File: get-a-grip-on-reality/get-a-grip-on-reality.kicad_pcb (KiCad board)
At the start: 2 copper layers, 100 x 100 mm, 87 parts, among them J1 Conn_01x04_Pin, J10 MOTOR4, J11 MOTOR5, J12 Battery Connector MCU, J13 Conn_01x05_Pin, J14 Conn_01x05_Pin, J15 Battery Connector Bat, J2 HALL1, J3 HALL2, J4 HALL3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

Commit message: fixes to pcb
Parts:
- added  : LOGO, Symbol:logo_shark, F.Cu at (108.3, 89.5)
- added P2: USB_C_Plug_USB2.0, Connector_USB:USB_C_Receptacle_GCT_USB4110, F.Cu at (123.3, 34.9)
- D8: moved to B.Cu
- moved D8 56.3 mm to (126.2, 42.3)
- moved R8 2.77 mm to (129.5, 53.7)
- moved D7 1.84 mm to (127.5, 54.6), turned to -90 degrees
- moved R12 0.46 mm to (121.3, 68.3)
- moved C24 0.45 mm to (121.3, 64.9)
- moved C21 0.11 mm to (122.2, 55.2)
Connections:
- C14 pad 1: +5V -> +5VUSB
- C28 pad 1: +5V -> +5VBuck
- C29 pad 1: +5V -> +5VBuck
- C30 pad 1: +5V -> +5VBuck
- D7 pad 2: GND -> +5VUSB
- D8 pad 2: +5V -> +5VUSB
- J15 pad 2: +5V -> +5VBuck
- L2 pad 2: +5V -> +5VBuck
- P1 pad A4: +5V -> +5V_USB_ESP
- P1 pad A9: +5V -> +5V_USB_ESP
- P1 pad B4: +5V -> +5V_USB_ESP
- P1 pad B9: +5V -> +5V_USB_ESP
- P1 pad S1: unconnected-(P1-SHIELD-PadS1) -> GND
- R19 pad 1: +5V -> +5VBuck
- U3 pad 4: +5V -> +5V_USB_ESP
- U3 pad 7: +5V -> +5V_USB_ESP
- U6 pad 23: +5V -> +5VUSB
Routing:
- net +5V: track 78.6 -> 0.00 mm, vias 5 -> 3
- net +5VUSB: track 0.00 -> 33.0 mm, vias 0 -> 1
- net +5VBuck: track 0.00 -> 15.9 mm, vias 0 -> 2
- net GND: track 36.3 -> 50.0 mm, vias 226 -> 221
- net +5V_USB_ESP: track 0.00 -> 10.2 mm
- net Net-(U6-STAT): track 3.69 -> 6.96 mm
- net Net-(D7-K): track 1.84 -> 2.77 mm
- net Net-(U6-BTST): track 13.8 -> 13.1 mm
- net Net-(U7-VCC): track 13.0 -> 12.4 mm
- net Net-(P2-D+): track 0.00 -> 0.50 mm
- net +BATT: vias 51 -> 50
- added copper zone on B.Cu, net +5VBuck

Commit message: add more shorks
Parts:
- added  : LOGO, Symbol:logo_shark, B.Cu at (54.3, 70.4)
- added  : LOGO, Symbol:logo_shark, B.Cu at (55.9, 47.5)
- added  : LOGO, Symbol:logo_shark, B.Cu at (68.8, 58.1)
- added  : LOGO, Symbol:logo_shark, B.Cu at (76.8, 39.5)
-  : moved to B.Cu
- turned   to 180 degrees
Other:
- board text added: "Get a Grip on Reality Sherwin Chiu Winston Lu Paul Kokhanov Chris Risebrough Andrew Droujinine"

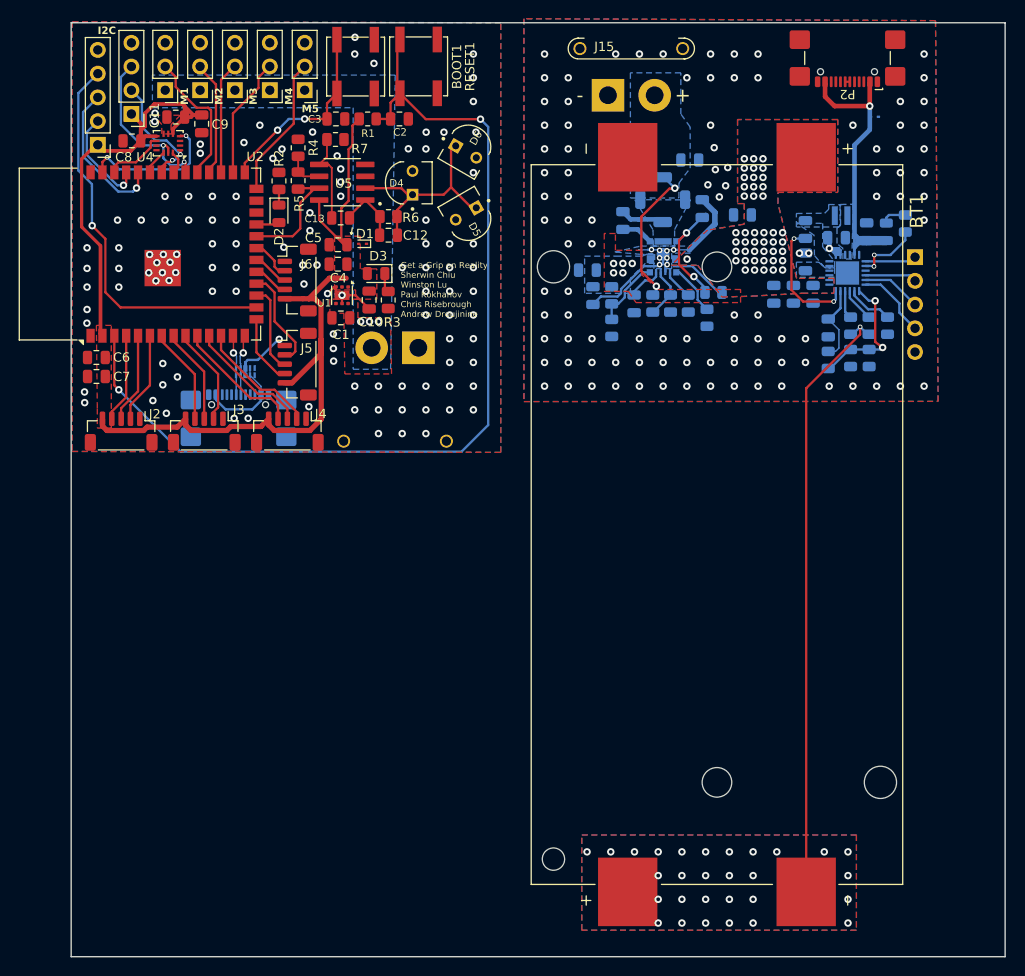
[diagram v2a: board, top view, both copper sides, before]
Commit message: add edge marks separately for pcbs
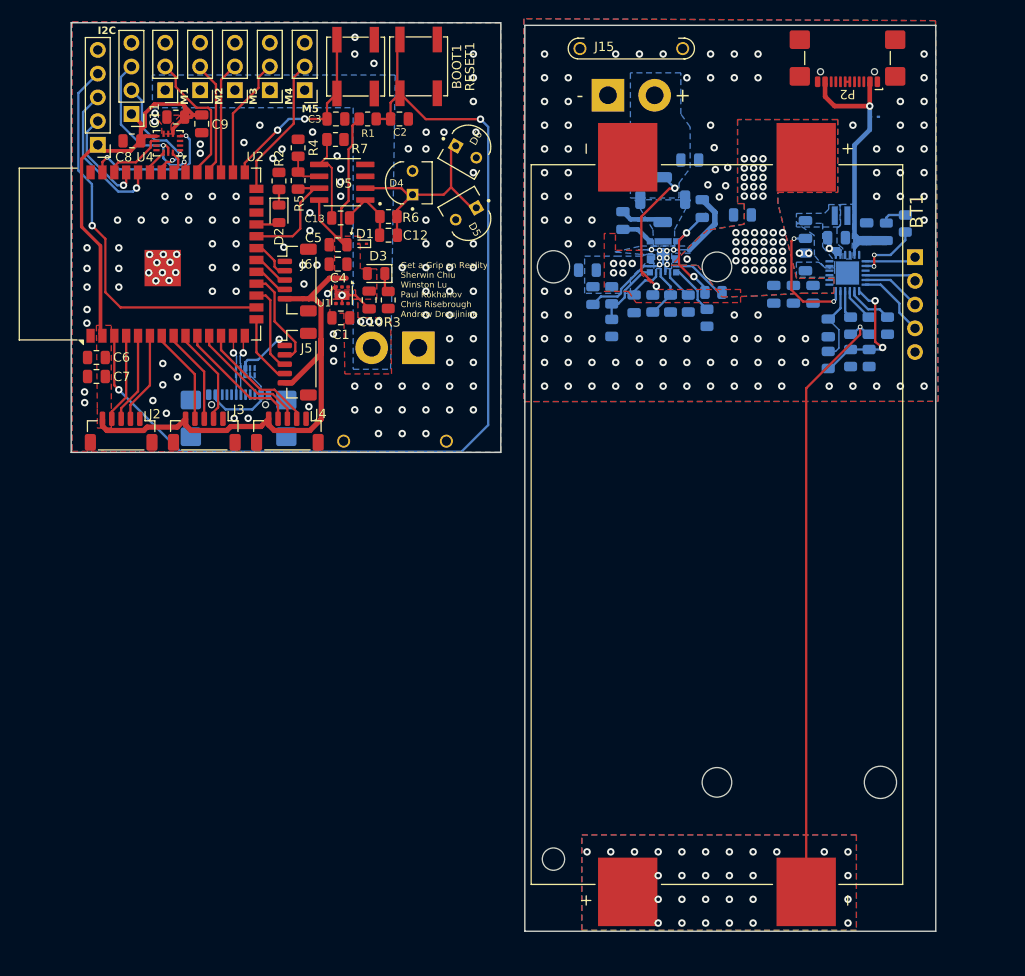
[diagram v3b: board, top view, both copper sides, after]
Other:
- board size 100 x 100 mm -> 92.6 x 97.3 mm
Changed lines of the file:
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@@
 	(gr_rect
 		(start 40.225 32.225)
-		(end 140.225 132.225)
+		(end 86.225 78.225)
 		(stroke
 			(width 0.15)
+			(type default)
+		)
+		(fill none)
+		(layer "Edge.Cuts")
+	)
+	(gr_rect
+		(start 88.8 32.5)
+		(end 132.8 129.5)
+		(stroke
+			(width 0.15)

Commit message: final version
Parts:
- removed the   at (108.3, 89.5)
- removed BT1: 1048P, fydp library:BAT_1048P
- removed C14, C16, C19: 1u, Capacitor_SMD:C_0805_2012Metric
- removed C15, C18, C24: 4.7u, Capacitor_SMD:C_0805_2012Metric
- removed C17, C20, C27: 100n, Capacitor_SMD:C_0805_2012Metric
- removed C21: 10u, Capacitor_SMD:C_0805_2012Metric
- removed C22: 2.2u, Capacitor_SMD:C_0805_2012Metric
- removed C23: 39n, Capacitor_SMD:C_0805_2012Metric
- removed C25: 47n, Capacitor_SMD:C_0805_2012Metric
- removed C26: 44u, Capacitor_SMD:C_0805_2012Metric
- removed C28, C29, C30: 47u, Capacitor_SMD:C_0805_2012Metric
- removed D7: LED, LED_SMD:LED_0805_2012Metric
- removed D8: ESD9B5.0ST5G, Diode_SMD:D_SOD-923
- removed J14: Conn_01x05_Pin, Connector_PinHeader_2.54mm:PinHeader_1x05_P2.54mm_Vertical
- removed J15: Battery Connector Bat, Connector_AMASS:AMASS_XT30PW-F_1x02_P2.50mm_Horizontal
- removed L1: 1u, Inductor_SMD:L_Taiyo-Yuden_MD-2020
- removed L2: 220u, Inductor_SMD:L_Bourns_SRU5016_5.2x5.2mm
- removed P2: USB_C_Plug_USB2.0, Connector_USB:USB_C_Receptacle_GCT_USB4110
- removed R10: 422k, Resistor_SMD:R_0805_2012Metric
- removed R11: 100k, Resistor_SMD:R_0805_2012Metric
- removed R12: 5.23k, Resistor_SMD:R_0805_2012Metric
- removed R13: 30.1k, Resistor_SMD:R_0805_2012Metric
- removed R14, R20, TH1: 10k, Resistor_SMD:R_0805_2012Metric
- removed R15: 11k, Resistor_SMD:R_0805_2012Metric
- removed R16: 5k, Resistor_SMD:R_0805_2012Metric
- removed R17: 300, Resistor_SMD:R_0805_2012Metric
- removed R18: 9.5, Resistor_SMD:R_0805_2012Metric
- removed R19: 45.3k, Resistor_SMD:R_0805_2012Metric
- removed R8: 2.2k, Resistor_SMD:R_0805_2012Metric
- removed R9: 383, Resistor_SMD:R_0805_2012Metric
- removed U6: BQ25887, Package_DFN_QFN:VQFN-24-1EP_4x4mm_P0.5mm_EP2.5x2.5mm
- removed U7: TPS54KB20RZRR, fydp:RZR0016A-MFG
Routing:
- net /Power/CELL_1: track 65.5 -> 0.00 mm, vias 30 -> 0
- net GND: track 50.0 -> 12.9 mm, vias 221 -> 120
- net +5VUSB: track 33.0 -> 0.00 mm, vias 1 -> 0
- net +5VBuck: track 15.9 -> 0.00 mm, vias 2 -> 0
- net Net-(U6-TS): track 14.0 -> 0.00 mm, vias 2 -> 0
- net Net-(U6-BTST): track 13.1 -> 0.00 mm, vias 2 -> 0
- net Net-(U7-VCC): track 12.4 -> 0.00 mm, vias 2 -> 0
- net Net-(U6-REGN): track 8.03 -> 0.00 mm
- net Net-(J14-Pin_4): track 7.81 -> 0.00 mm
- net Net-(U7-EN): track 7.60 -> 0.00 mm
- net Net-(U6-STAT): track 6.96 -> 0.00 mm, vias 2 -> 0
- net Net-(J14-Pin_3): track 6.39 -> 0.00 mm
- net Net-(U7-PG): track 6.10 -> 0.00 mm
- net Net-(J14-Pin_2): track 5.54 -> 0.00 mm
- net Net-(U7-MSEL): track 5.50 -> 0.00 mm
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- removed copper zone on B.Cu, net +5VBuck
- removed copper zone on B.Cu, net +BATT
- removed copper zone on F.Cu, net +BATT
- removed copper zone on B.Cu, net /Power/CELL_1
- removed copper zone on F.Cu, net /Power/CELL_1
- removed copper zone on B.Cu, net /Power/PMID
- removed copper zone on B.Cu, net /Power/SNS
- removed copper zone on B.Cu, net /Power/SW_5
- removed copper zone on B.Cu, net /Power/SW_BAT
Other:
- board size 92.6 x 97.3 mm -> 46 x 46 mm

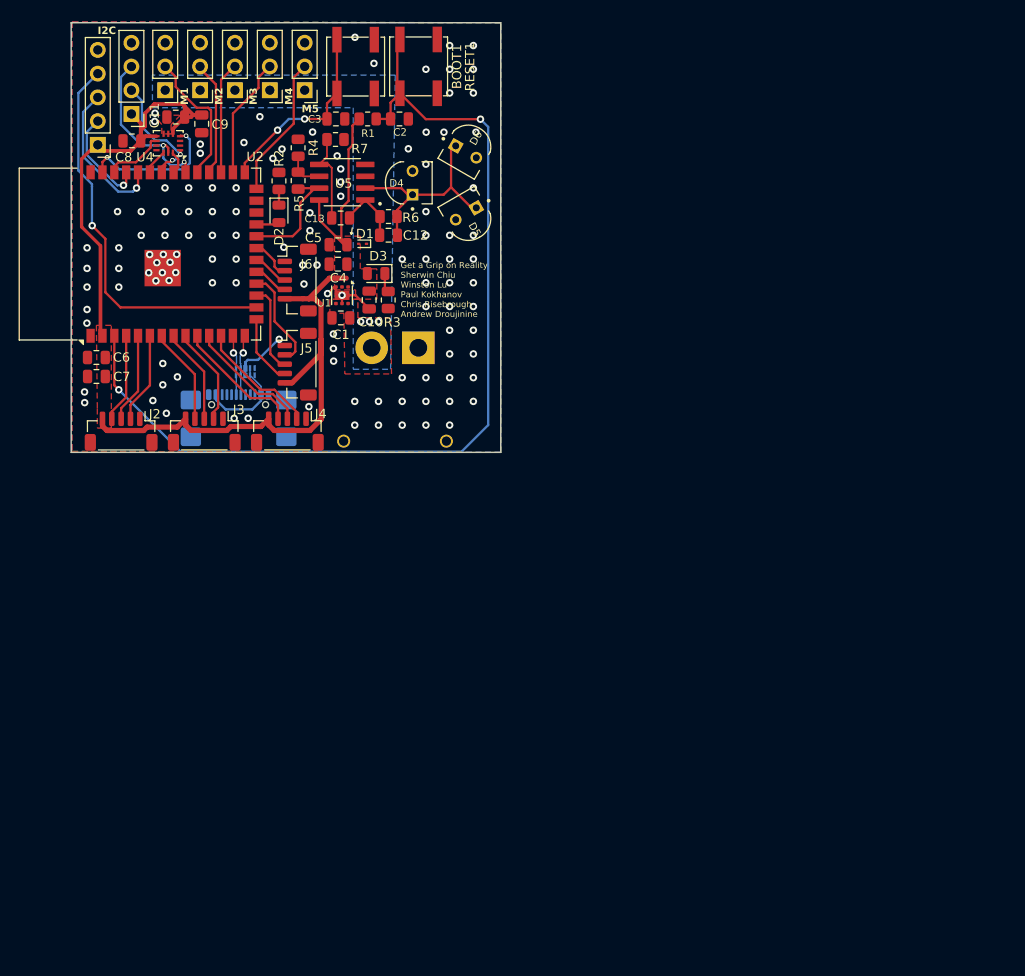
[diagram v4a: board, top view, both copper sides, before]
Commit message: add test.ino for ble and imu test
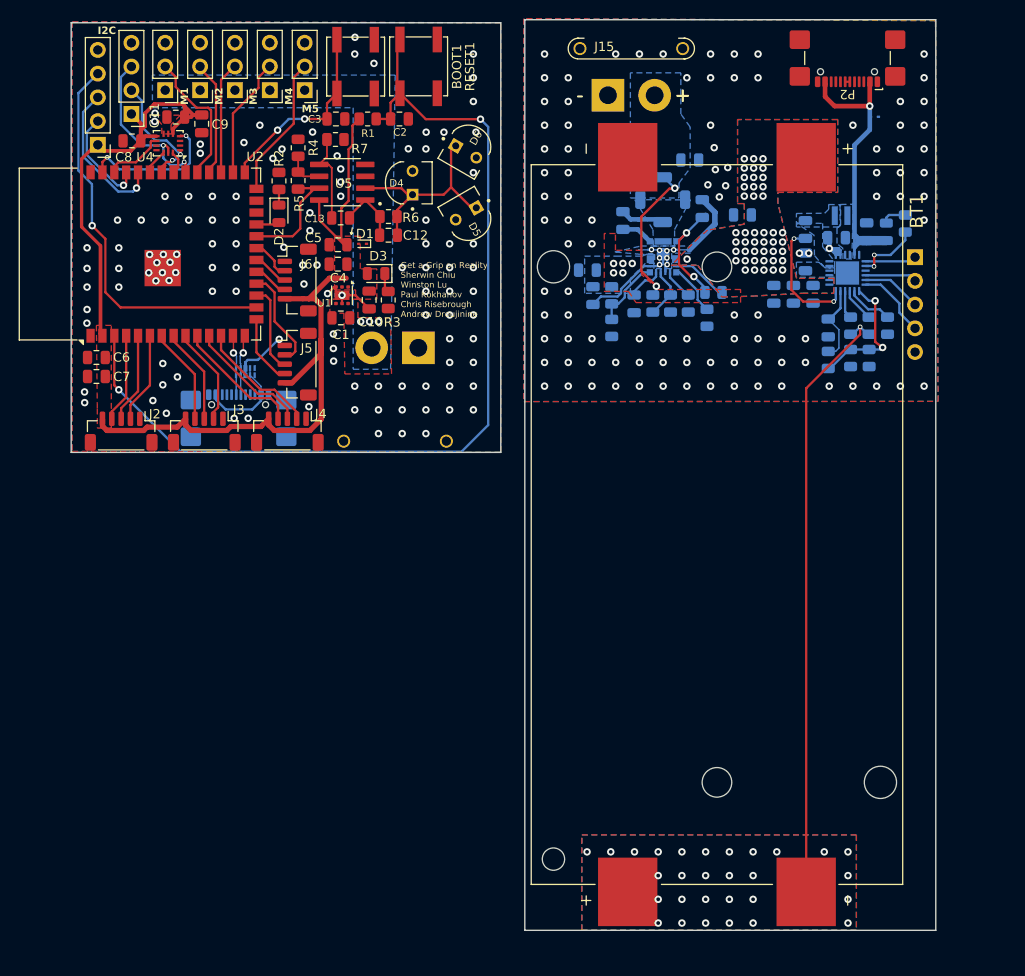
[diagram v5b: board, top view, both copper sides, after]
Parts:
- added  : LOGO, Symbol:logo_shark, B.Cu at (108.3, 89.5)
- added BT1: 1048P, fydp library:BAT_1048P, F.Cu at (109.4, 86.0)
- added C14: 1u, Capacitor_SMD:C_0805_2012Metric, B.Cu at (125.4, 54.6)
- added C15: 4.7u, Capacitor_SMD:C_0805_2012Metric, B.Cu at (119.7, 61.3)
- added C16: 1u, Capacitor_SMD:C_0805_2012Metric, B.Cu at (117.6, 61.3)
- added C17: 100n, Capacitor_SMD:C_0805_2012Metric, B.Cu at (96.1, 61.4)
- added C18: 4.7u, Capacitor_SMD:C_0805_2012Metric, B.Cu at (95.5, 58.7)
- added C19: 1u, Capacitor_SMD:C_0805_2012Metric, B.Cu at (115.5, 61.3)
- added C20: 100n, Capacitor_SMD:C_0805_2012Metric, B.Cu at (112.1, 52.8)
- added C21: 10u, Capacitor_SMD:C_0805_2012Metric, B.Cu at (122.2, 55.2)
- added C22: 2.2u, Capacitor_SMD:C_0805_2012Metric, B.Cu at (107.8, 52.1)
- added C23: 39n, Capacitor_SMD:C_0805_2012Metric, B.Cu at (100.5, 62.3)
- added C24: 4.7u, Capacitor_SMD:C_0805_2012Metric, B.Cu at (121.3, 64.9)
- added C25: 47n, Capacitor_SMD:C_0805_2012Metric, B.Cu at (118.8, 54.4)
- added C26: 44u, Capacitor_SMD:C_0805_2012Metric, B.Cu at (118.8, 57.8)
- added C27: 100n, Capacitor_SMD:C_0805_2012Metric, B.Cu at (99.3, 53.4)
- added C28: 47u, Capacitor_SMD:C_0805_2012Metric, B.Cu at (106.5, 46.9)
- added C29: 47u, Capacitor_SMD:C_0805_2012Metric, B.Cu at (100.2, 47.0)
- added C30: 47u, Capacitor_SMD:C_0805_2012Metric, B.Cu at (100.2, 45.0)
- added D7: LED, LED_SMD:LED_0805_2012Metric, B.Cu at (127.5, 54.6)
- added D8: ESD9B5.0ST5G, Diode_SMD:D_SOD-923, B.Cu at (126.2, 42.3)
- added J14: Conn_01x05_Pin, Connector_PinHeader_2.54mm:PinHeader_1x05_P2.54mm_Vertical, B.Cu at (130.6, 57.3)
- added J15: Battery Connector Bat, Connector_AMASS:AMASS_XT30PW-F_1x02_P2.50mm_Horizontal, F.Cu at (97.7, 40.0)
- added L1: 1u, Inductor_SMD:L_Taiyo-Yuden_MD-2020, B.Cu at (122.7, 52.9)
- added L2: 220u, Inductor_SMD:L_Bourns_SRU5016_5.2x5.2mm, B.Cu at (103.6, 51.2)
- added P2: USB_C_Plug_USB2.0, Connector_USB:USB_C_Receptacle_GCT_USB4110, F.Cu at (123.3, 34.9)
- added R10: 422k, Resistor_SMD:R_0805_2012Metric, B.Cu at (98.1, 61.4)
- added R11: 100k, Resistor_SMD:R_0805_2012Metric, B.Cu at (98.1, 64.9)
- added R12: 5.23k, Resistor_SMD:R_0805_2012Metric, B.Cu at (121.3, 68.3)
- added R13: 30.1k, Resistor_SMD:R_0805_2012Metric, B.Cu at (123.7, 68.1)
- added R14: 10k, Resistor_SMD:R_0805_2012Metric, B.Cu at (109.0, 61.1)
- added R15: 11k, Resistor_SMD:R_0805_2012Metric, B.Cu at (106.3, 62.3)
- added R16: 5k, Resistor_SMD:R_0805_2012Metric, B.Cu at (108.3, 63.8)
- added R17: 300, Resistor_SMD:R_0805_2012Metric, B.Cu at (125.7, 64.7)
- added R18: 9.5, Resistor_SMD:R_0805_2012Metric, B.Cu at (123.7, 64.7)
- added R19: 45.3k, Resistor_SMD:R_0805_2012Metric, B.Cu at (102.5, 62.3)
- added R20: 10k, Resistor_SMD:R_0805_2012Metric, B.Cu at (104.4, 62.3)
- added R8: 2.2k, Resistor_SMD:R_0805_2012Metric, B.Cu at (129.5, 53.7)
- added R9: 383, Resistor_SMD:R_0805_2012Metric, B.Cu at (127.6, 64.7)
- added TH1: 10k, Resistor_SMD:R_0805_2012Metric, B.Cu at (125.7, 68.1)
- added U6: BQ25887, Package_DFN_QFN:VQFN-24-1EP_4x4mm_P0.5mm_EP2.5x2.5mm, B.Cu at (123.3, 59.0)
- added U7: TPS54KB20RZRR, fydp:RZR0016A-MFG, B.Cu at (103.6, 57.3)
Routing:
- net /Power/CELL_1: track 0.00 -> 65.5 mm, vias 0 -> 30
- net GND: track 12.9 -> 50.0 mm, vias 120 -> 221
- net +5VUSB: track 0.00 -> 33.0 mm, vias 0 -> 1
- net +5VBuck: track 0.00 -> 15.9 mm, vias 0 -> 2
- net Net-(U6-TS): track 0.00 -> 14.0 mm, vias 0 -> 2
- net Net-(U6-BTST): track 0.00 -> 13.1 mm, vias 0 -> 2
- net Net-(U7-VCC): track 0.00 -> 12.4 mm, vias 0 -> 2
- net Net-(U6-REGN): track 0.00 -> 8.03 mm
- net Net-(J14-Pin_4): track 0.00 -> 7.81 mm
- net Net-(U7-EN): track 0.00 -> 7.60 mm
- net Net-(U6-STAT): track 0.00 -> 6.96 mm, vias 0 -> 2
- net Net-(J14-Pin_3): track 0.00 -> 6.39 mm
- net Net-(U7-PG): track 0.00 -> 6.10 mm
- net Net-(J14-Pin_2): track 0.00 -> 5.54 mm
- net Net-(U7-MSEL): track 0.00 -> 5.50 mm
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- added copper zone on B.Cu, net +5VBuck
- added copper zone on B.Cu, net +BATT
- added copper zone on F.Cu, net +BATT
- added copper zone on B.Cu, net /Power/CELL_1
- added copper zone on F.Cu, net /Power/CELL_1
- added copper zone on B.Cu, net /Power/PMID
- added copper zone on B.Cu, net /Power/SNS
- added copper zone on B.Cu, net /Power/SW_5
- added copper zone on B.Cu, net /Power/SW_BAT
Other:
- board size 46 x 46 mm -> 92.6 x 97.5 mm
- board text added: "+"
- board text added: "-"
